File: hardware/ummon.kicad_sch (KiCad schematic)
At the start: 29 parts, among them J1 Conn_01x08_Pin, J2 Conn_01x05_Pin, J3 Conn_01x04_Pin, J4 Conn_01x04_Pin, SW1 Reboot, SW2 Flash, U1 ESP32-C6-WROOM-1-N8, U2 SCD41-D-R2, U3 SGP41-D-R4, U4 SHT41-AD1B-R2

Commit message: :sparkles: Add voltage regulators
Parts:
- added C14, C19: 10µF, symbol Device:C_Small
- added C15, C16, C18, C20: 100nF, symbol Device:C_Small
- added C17, C21: 22µF tantalum, symbol Device:C_Small
- added F1: Polyfuse_Small, symbol Device:Polyfuse_Small
- added R2, R3: 5.1kΩ, symbol Device:R_Small
- added U5, U6: AMS1117-3.3, parts:SOT-223-3_L6.5-W3.4-P2.30-LS7.0-BR, symbol parts:AMS1117-3.3
- added USB1: TYPE-C 16PIN 2MD, parts:USB-C-SMD_TYPE-C-16PIN-2MD-073, symbol parts:TYPE-C16PIN2MD
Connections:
- net +3.3V: now also C16.1, C17.1, U5.2 (VOUT), U5.4 (VOUT); no longer C1.1, C3.1, C4.1, C5.1, C6.1, R1.1, U2.19 (VDDH), U2.7 (VDD), U3.5 (VDDH), U4.3 (VDD)
- net +5V: now also C14.1, C15.1, C18.1, C19.1, F1.2, U5.3 (VIN), U6.3 (VIN)
- net GND: now also C14.2, C15.2, C16.2, C17.2, C18.2, C19.2, C20.2, C21.2, R2.2, R3.2, U5.1 (GND), U6.1 (GND), USB1.13 (EH), USB1.14 (EH), USB1.A1B12 (GND), USB1.B1A12 (GND)
- net USB_D+: now also USB1.A6 (Dp1), USB1.B6 (Dp2)
- net USB_D-: now also USB1.A7 (Dn1), USB1.B7 (Dn2)
- new net: F1.1, USB1.A4B9 (VBUS), USB1.B4A9 (VBUS)
- new net: R2.1, USB1.A5 (CC1)
- new net: R3.1, USB1.B5 (CC2)
- new net +3.3V_SNSR: C1.1, C20.1, C21.1, C3.1, C4.1, C5.1, C6.1, R1.1, U2.19 (VDDH), U2.7 (VDD), U3.5 (VDDH), U4.3 (VDD), U6.2 (VOUT), U6.4 (VOUT)
- no-connect marks 15 -> 17
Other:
- moved on the sheet: C12, C13, C8, C9, J1, J2, J3, J4, R4, R6, R7, U1

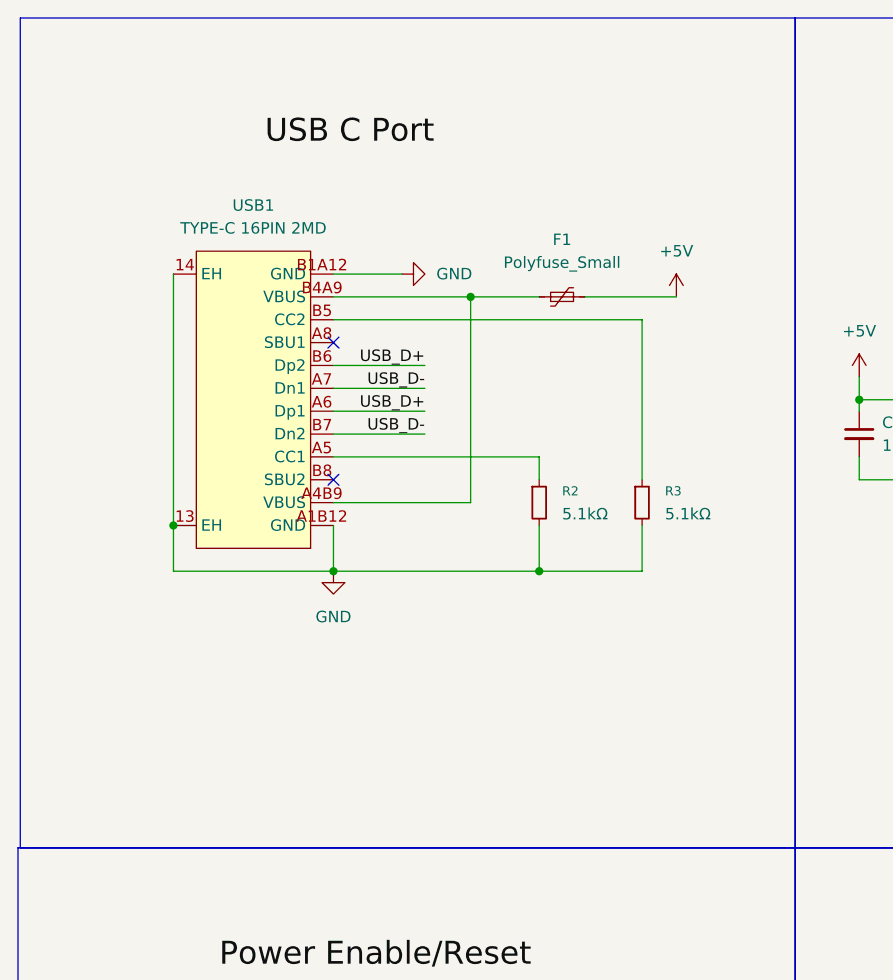
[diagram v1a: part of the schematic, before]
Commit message: :sparkles: USB is now ESD protected
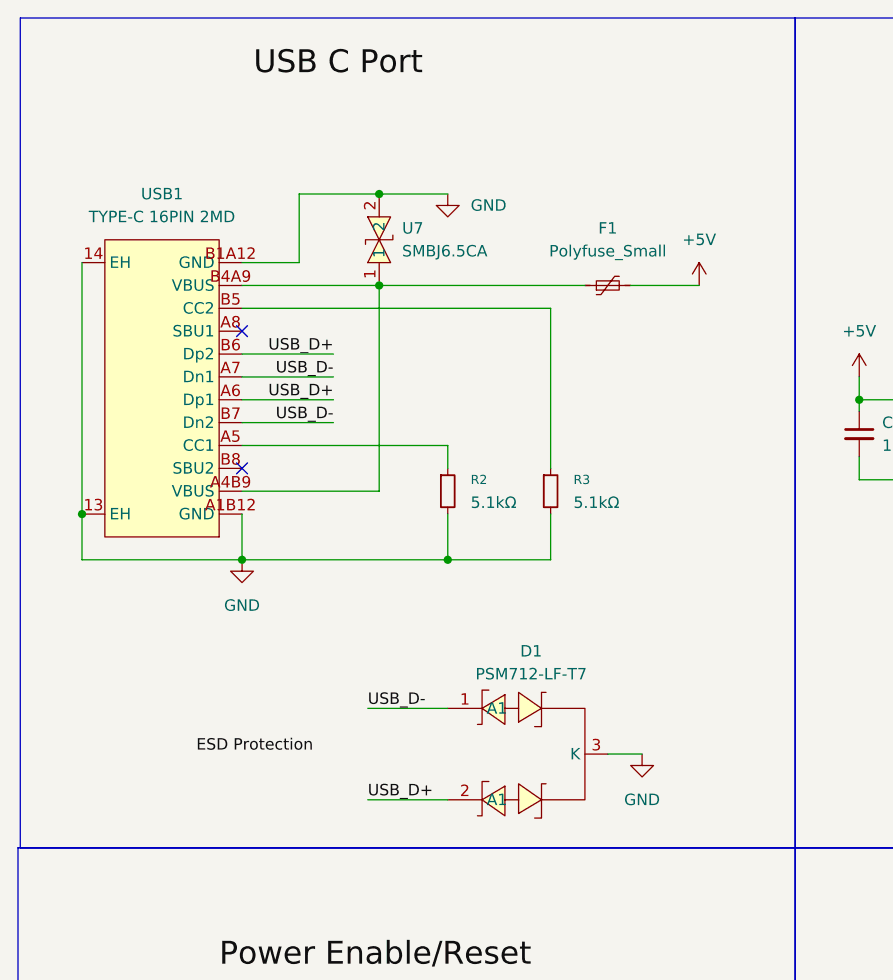
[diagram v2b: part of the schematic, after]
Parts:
- added D1: PSM712-LF-T7, parts:SOT-23-3_L3.0-W1.7-P0.95-LS2.9-BR, symbol parts:PSM712-LF-T7
- added U7: SMBJ6.5CA, parts:SMB_L4.6-W3.5-LS5.3-BI, symbol parts:SMBJ6.5CA_C7420377
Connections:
- net GND: now also D1.3 (K), U7.2
- net USB_D+: now also D1.2 (A1)
- net USB_D-: now also D1.1 (A1)
- net at F1.1, USB1.A4B9 (VBUS), USB1.B4A9 (VBUS): now also U7.1
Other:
- moved on the sheet: F1, R2, R3, USB1

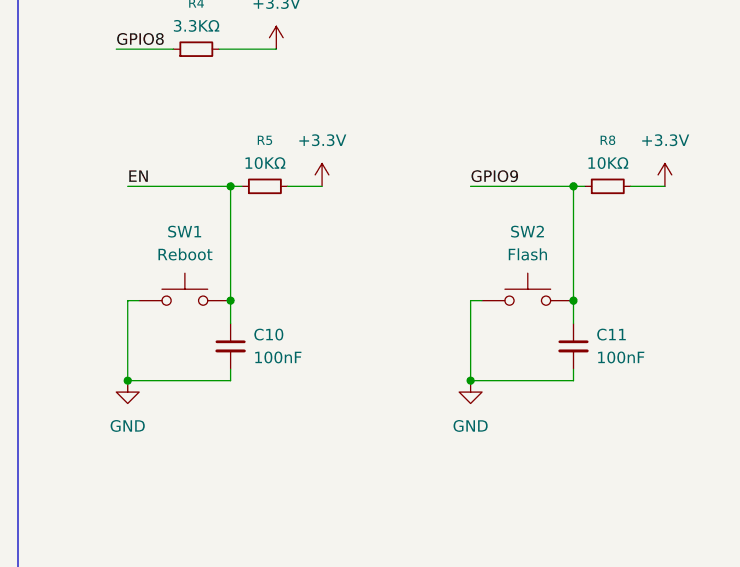
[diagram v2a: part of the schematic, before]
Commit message: :recycle: Uses correct buttons now
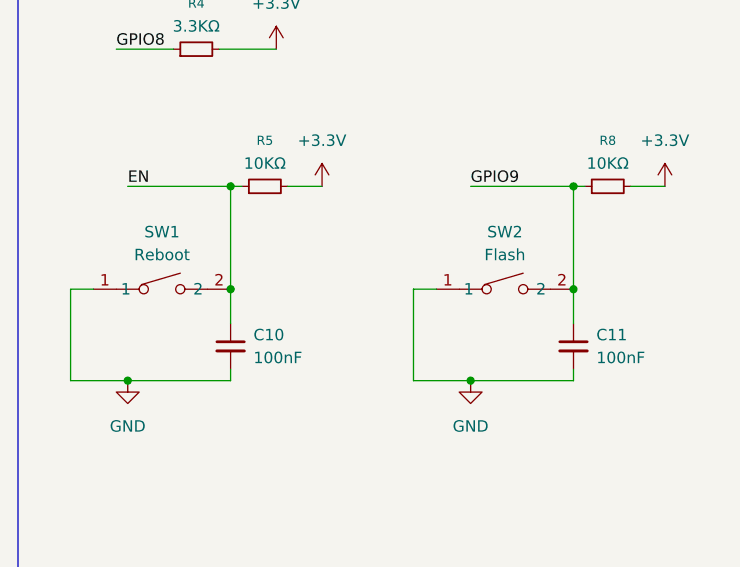
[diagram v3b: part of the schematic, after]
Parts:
- removed SW1: Reboot, symbol Switch:SW_Push
- removed SW2: Flash, symbol Switch:SW_Push
- added SW1: Reboot, parts:SW-SMD_L3.9-W3.0-P4.45, symbol parts:TS-1088-AR02016
- added SW2: Flash, parts:SW-SMD_L3.9-W3.0-P4.45, symbol parts:TS-1088-AR02016
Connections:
- net EN: now also SW1.2
- net GND: now also SW1.1, SW2.1
- net GPIO9: now also SW2.2

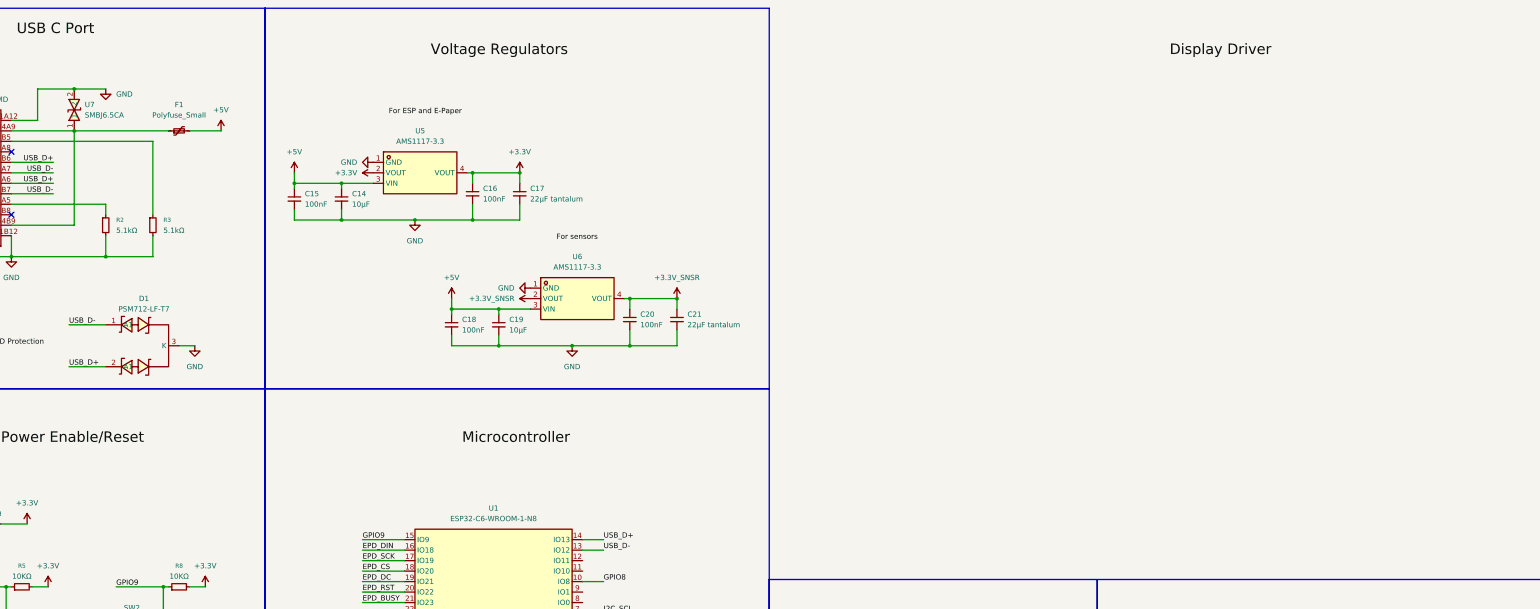
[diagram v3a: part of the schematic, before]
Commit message: :sparkles: Add edp driver
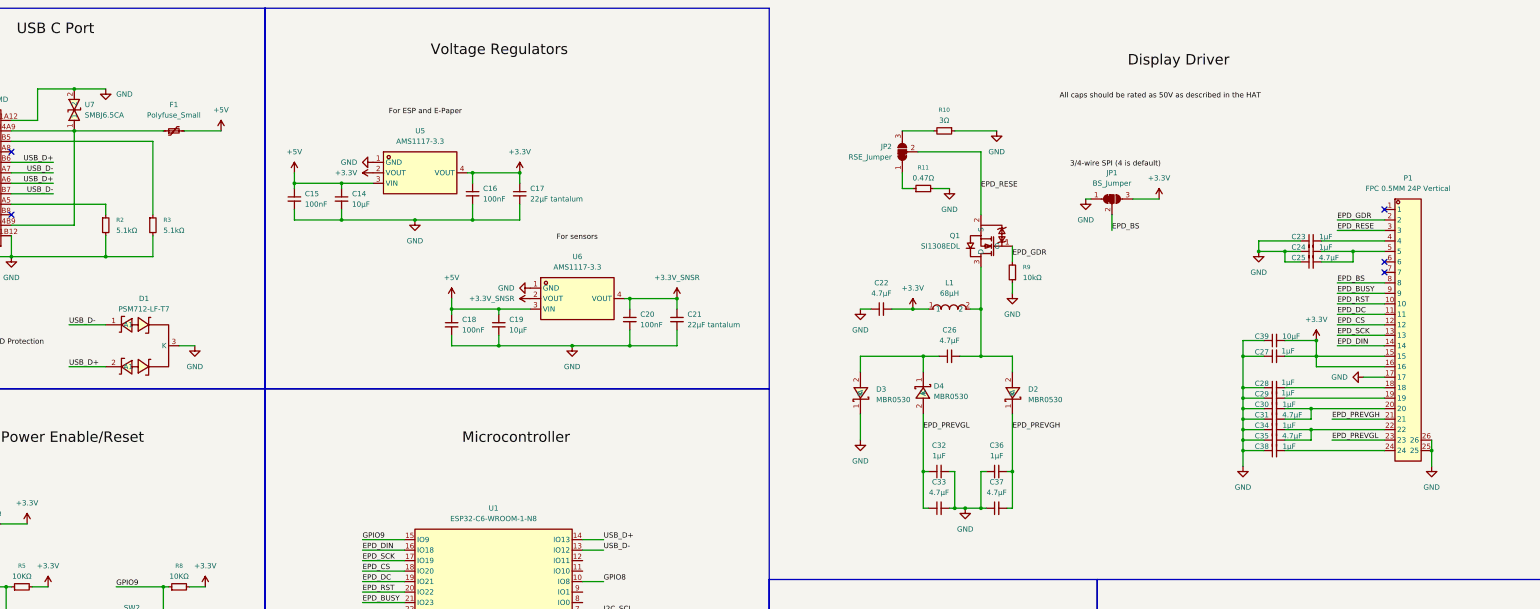
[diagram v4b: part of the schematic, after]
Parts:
- added C22, C25, C26, C31, C33, C35, C37: 4.7μF, symbol Device:C_Small
- added C23, C24, C27, C28, C29, C30, C32, C34, C36, C38: 1μF, symbol Device:C_Small
- added C39: 10μF, symbol Device:C_Small
- added D2, D3, D4: MBR0530, parts:SOD-123_L2.8-W1.8-LS3.7-RD, symbol parts:LMBR0530T1G
- added JP1: BS_Jumper, Jumper:SolderJumper-3_P1.3mm_Bridged12_RoundedPad1.0x1.5mm_NumberLabels, symbol Jumper:SolderJumper_3_Bridged12
- added JP2: RSE_Jumper, Jumper:SolderJumper-3_P1.3mm_Bridged12_RoundedPad1.0x1.5mm_NumberLabels, symbol Jumper:SolderJumper_3_Bridged12
- added L1: 68μH, parts:IND-SMD_L11.6-W10.1, symbol parts:CYA1040-68UH
- added P1: FPC 0.5MM 24P Vertical, parts:FPC-SMD_AFC11-S24ICC-00, symbol parts:FPC0.5MM24PVerticalmountingtypeH2.0mm
- added Q1: SI1308EDL, parts:SOT-323_L2.0-W1.3-P1.30-LS2.1-BR, symbol parts:SI1308EDL-T1-GE3
- added R10: 3Ω, symbol Device:R_Small
- added R11: 0.47Ω, symbol Device:R_Small
- added R9: 10kΩ, symbol Device:R_Small
- J1: footprint (none) -> Connector_PinHeader_2.54mm:PinHeader_1x08_P2.54mm_Vertical
- J2: footprint (none) -> Connector_PinHeader_2.54mm:PinHeader_1x05_P2.54mm_Vertical
- J3, J4: footprint (none) -> Connector_PinHeader_2.54mm:PinHeader_1x04_P2.54mm_Vertical
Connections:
- net +3.3V: now also C22.2, C27.2, C39.2, JP1.3 (B), L1.1, P1.15, P1.16
- net EPD_BUSY: now also P1.9
- net EPD_CS: now also P1.12
- net EPD_DC: now also P1.11
- net EPD_DIN: now also P1.14
- net EPD_RST: now also P1.10
- net EPD_SCK: now also P1.13
- net GND: now also C22.1, C23.1, C24.1, C25.1, C27.1, C28.1, C29.1, C30.1, C31.1, C32.2, C33.2, C34.1, C35.1, C36.1, C37.1, C38.1, C39.1, D3.1 (K), JP1.1 (A), P1.17, P1.25, P1.26, R10.1, R11.2, R9.1
- new net: JP2.1 (A), R11.1
- new net: JP2.3 (B), R10.2
- new net: C26.1, D3.2 (A), D4.1 (K)
- new net: C34.2, C35.2, P1.22
- new net: C30.2, C31.2, P1.20
- new net: C28.2, P1.18
- new net: C24.2, C25.2, P1.5
- new net: C29.2, P1.19
- new net: C38.2, P1.24
- new net: C23.2, P1.4
- new net: C26.2, D2.2 (A), L1.2, Q1.3 (D)
- new net EPD_BS: JP1.2 (C), P1.8
- new net EPD_GDR: P1.2, Q1.1 (G), R9.2
- new net EPD_PREVGH: C36.2, C37.2, D2.1 (K), P1.21
- new net EPD_PREVGL: C32.1, C33.1, D4.2 (A), P1.23
- new net EPD_RESE: JP2.2 (C), P1.3, Q1.2 (S)
- no-connect marks 17 -> 20
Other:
- moved on the sheet: F1
